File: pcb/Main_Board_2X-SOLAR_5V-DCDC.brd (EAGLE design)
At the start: 86.4 x 52.1 mm, 89 parts, among them CN1 DCIN, CN5 USBA_FEMALE, CN6 MicroUSB, IC1 MCP73871, IC2 MCP73871, T2 MMUN2133LT1G, U3 TPS61090RSAR

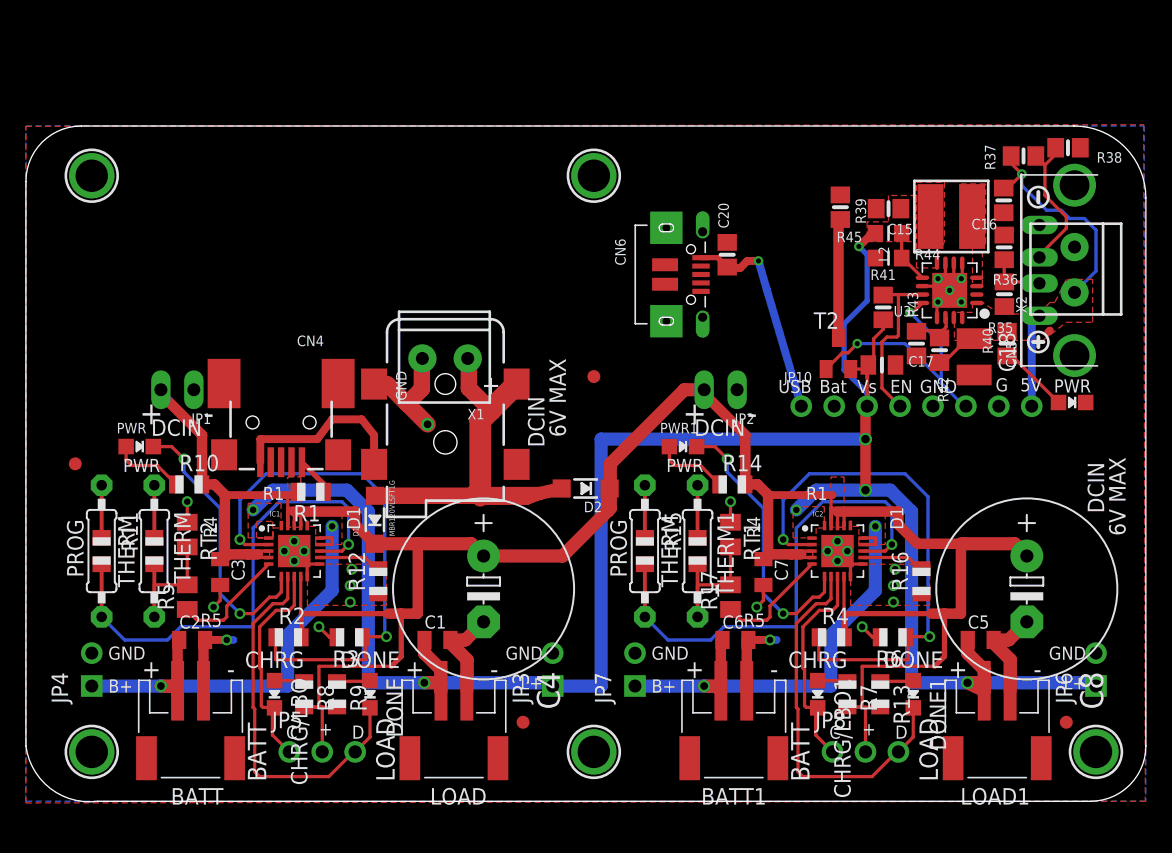
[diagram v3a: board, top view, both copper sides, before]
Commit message: Rev 2 start
Removed extra USB mounts, jumpers, and headers. BOM completed but missing a couple items from Digikey
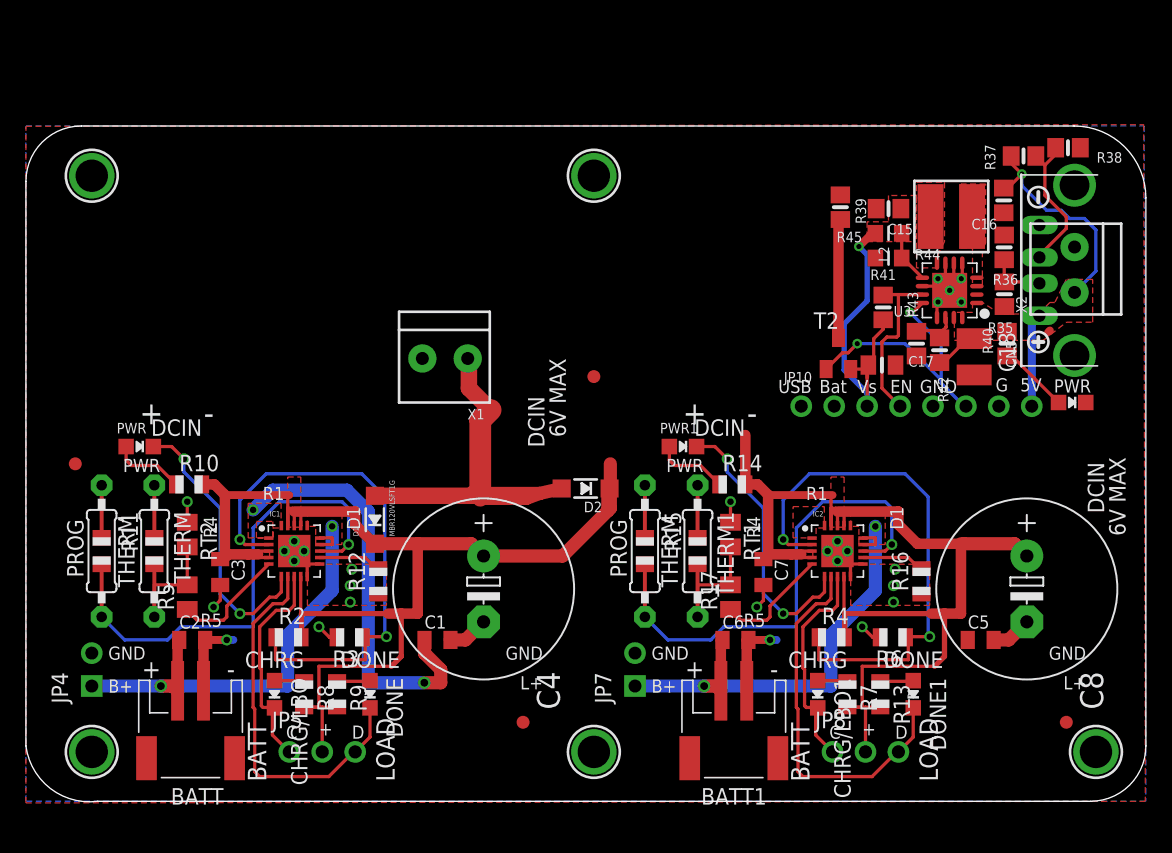
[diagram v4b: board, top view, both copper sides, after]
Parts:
- removed C20: 10uF, microbuilder:0805-NO
- removed CN1: DCIN, microbuilder:DCJACK_2MM_SMT
- removed CN4: (no value), microbuilder:USB-MINIB_LARGER
- removed CN6: MicroUSB, microbuilder:4UCONN_20329
- removed JP1, JP2: DCIN, microbuilder:1X02_OVAL
- removed JP3, JP6: LOAD, microbuilder:1X02_ROUND
- removed LOAD, LOAD1: (no value), adafruit:JST-PH-2-SMT-RA
- removed R1: 0, adafruit:R0805
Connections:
- removed net GNDBREAK: CN1.GNDBREAK, CN4.GND, CN4.GND1, CN4.GND2, CN4.GND3, CN4.GND4
- removed net N$2: CN4.VBUS, R1.1
- net GND: no longer C20.2, CN1.GND, CN6.BASE@1, CN6.BASE@2, CN6.GND, CN6.SPRT@1, CN6.SPRT@2, CN6.SPRT@3, CN6.SPRT@4, JP1.1, JP2.1, JP3.2, JP6.2, LOAD.2, LOAD1.2
- net PV_IN: no longer CN1.PWR
- net VBAT: no longer JP3.1, JP6.1, LOAD.1, LOAD1.1
- net VBUS: no longer C20.1, CN6.VBUS
- net VCC: no longer JP1.2, JP2.2, R1.2
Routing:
- net VBAT: track 162.8 -> 57.3 mm, vias 7 -> 3
- net GND: track 68.9 -> 44.9 mm, vias 23 -> 22
- net VCC: track 209.3 -> 186.2 mm
- net VBUS: track 16.7 -> 0.00 mm, vias 1 -> 0
- net GNDBREAK: track 14.3 -> 0.00 mm
- net N$2: track 2.98 -> 0.00 mm
- net PV_IN: track 34.4 -> 31.5 mm

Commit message: Part removal and gitignore update
removed more jumpers and headers and updated the ignore file to ignore autosave files
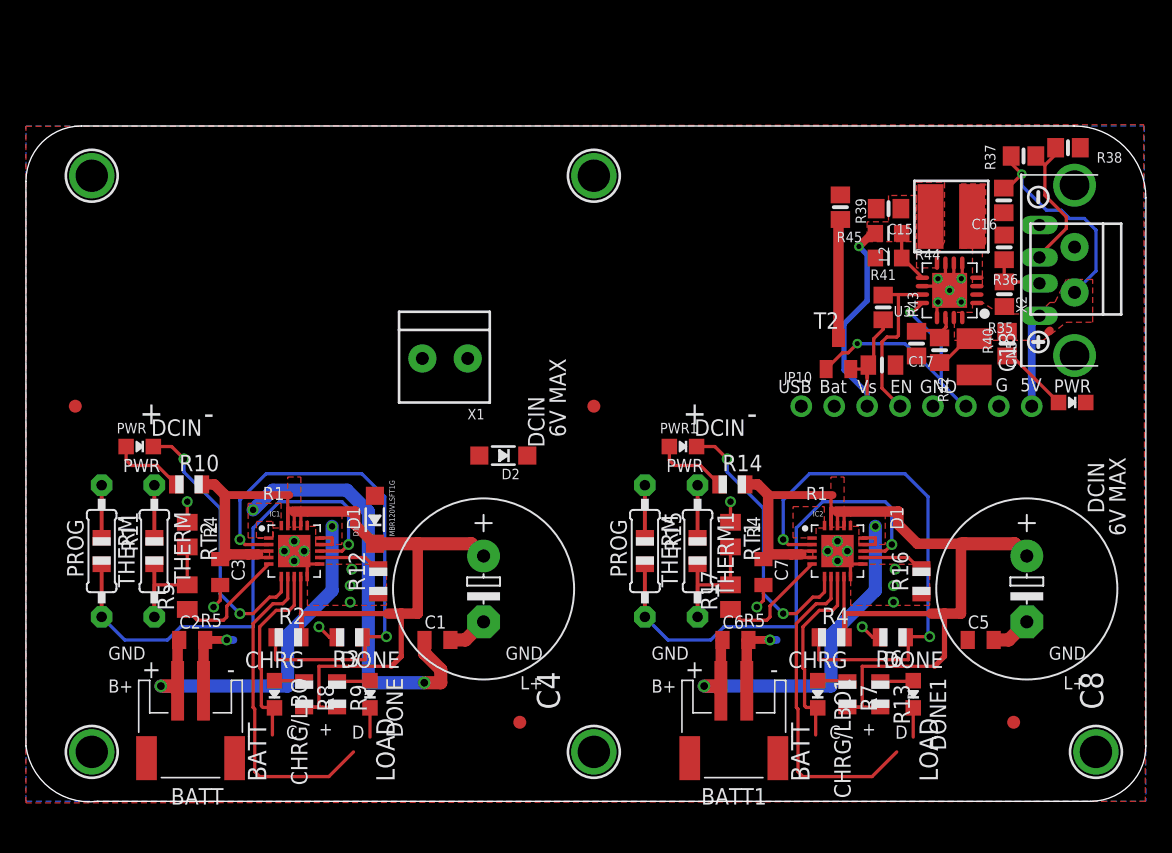
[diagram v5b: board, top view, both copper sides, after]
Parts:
- removed JP4, JP7: BATT, microbuilder:1X02_ROUND
- removed JP5, JP8: (no value), adafruit:1X03-CLEANBIG
- moved D2 6.84 mm to (36.8, 26.7)
- moved U$2 4.45 mm to (3.81, 30.5)
- moved U$10 4.06 mm to (76.2, 6.10)
- moved U$8 2.29 mm to (43.8, 30.5)
- moved U$3 0.25 mm to (38.1, 6.10)
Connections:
- net BATT: no longer JP4.1
- net BATT1: no longer JP7.1
- net GND: no longer JP4.2, JP7.2
- net N$11: no longer JP5.1
- net N$17: no longer JP8.3
- net N$18: no longer JP8.1
- net N$4: no longer JP5.3
- net VCC: no longer JP5.2, JP8.2
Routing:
- net PV_IN: track 31.5 -> 0.00 mm
- net VCC: track 186.2 -> 159.0 mm
- net BATT1: track 37.0 -> 31.7 mm
- net BATT: track 37.0 -> 31.7 mm
- net N$11: track 16.8 -> 15.0 mm
- net N$18: track 16.8 -> 15.0 mm
- net N$4: track 29.2 -> 27.5 mm
- net N$17: track 29.2 -> 27.5 mm

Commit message: Added jumpers and diodes to load line regulation
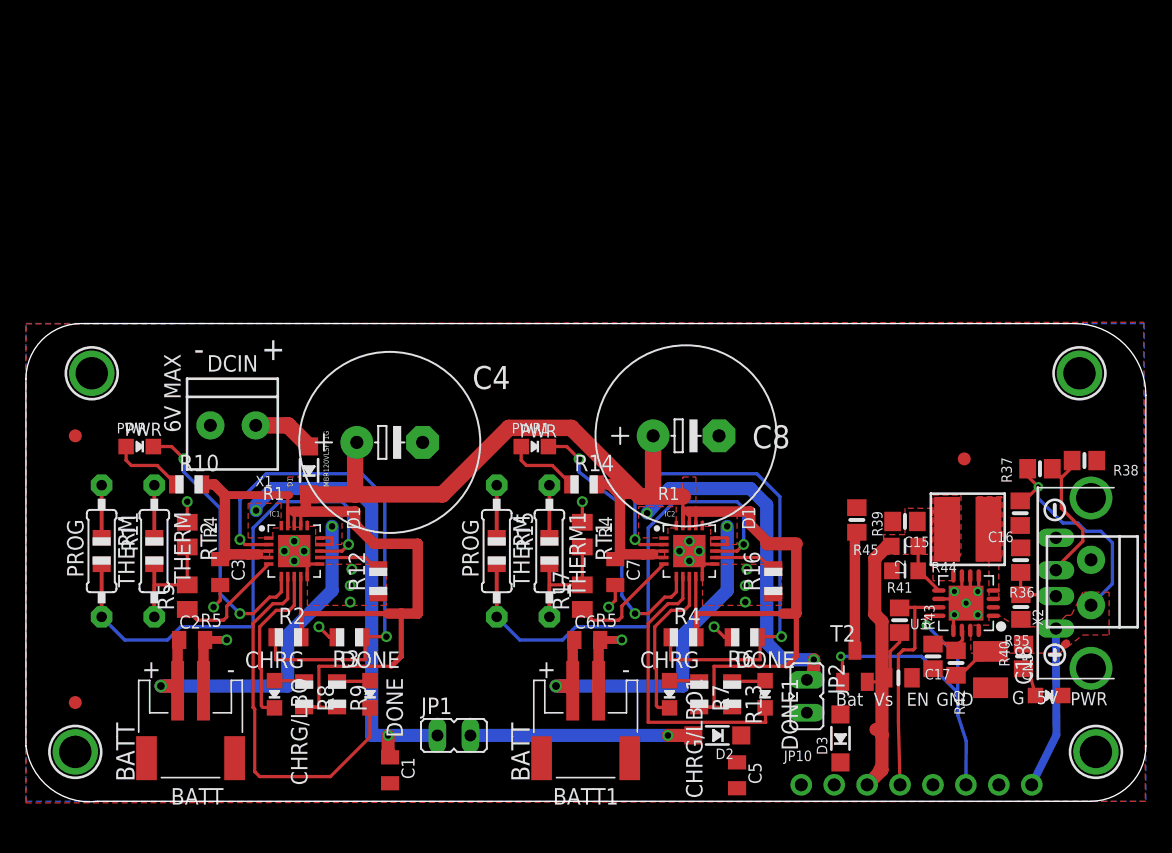
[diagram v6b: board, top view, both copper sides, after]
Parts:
- removed U$2: FIDUCIAL, adafruit:FIDUCIAL_1MM
- removed U$5, U$7: MOUNTINGHOLE2.5, microbuilder:MOUNTINGHOLE_2.5_PLATED
- added D3: MBR120VLSFT1G, microbuilder:SOD-123
- added JP1, JP2: (no value), jumper:JP1
- added U$1: MOUNTINGHOLE2.5, microbuilder:MOUNTINGHOLE_2.5_PLATED
- BATT, BATT1: value (none) -> 3.7V Li-ion
- JP10: value (none) -> 5V step up jumpers
- X1: value (none) -> Solar input
- X2: value (none) -> 5V output
- moved U$10 75.7 mm to (3.81, 28.2)
- moved U$8 46.1 mm to (3.81, 7.62)
- moved U$3 39.9 mm to (72.4, 26.4)
- moved JP10 29.2 mm to (68.7, 1.27)
- moved C8 28.8 mm to (50.9, 28.2), turned to 0 degrees
- moved D2 27.2 mm to (53.3, 5.08)
- moved C17 24.2 mm to (67.3, 9.53)
- moved CN5 24.2 mm to (86.0, 16.8)
- moved R42 24.2 mm to (71.8, 10.7)
- moved U$87 24.2 mm to (79.4, 22.5)
- moved X2 24.2 mm to (82.2, 16.8)
- moved C15 24.2 mm to (67.8, 21.6)
- moved C18 24.2 mm to (74.4, 10.2)
- moved R37 24.2 mm to (78.2, 25.7)
- moved R39 24.2 mm to (64.1, 21.7)
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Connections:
- net LBO renamed T2-BASE_LBO
- net N$1 renamed PG
- net N$11 renamed STAT1
- net N$15 renamed PROG3
- net N$16 renamed PROG1
- net N$17 renamed STAT2_1
- net N$18 renamed STAT1_1
- net N$22 renamed PROG3_1
- net N$23 renamed PROG1_1
- net N$26 renamed T2-DRAIN
- net N$4 renamed STAT2
- net N$9 renamed PG_1
- new net N$1: D3.A, JP2.2
- new net N$2: D2.A, JP1.2
- new net VOUT: C1.1, IC1.P$1, IC1.P$20, JP1.1
- new net VOUT1: C5.1, IC2.P$1, IC2.P$20, JP2.1
- net PV_IN: no longer D2.A
- net VBAT: now also D2.C, D3.C; no longer C1.1, C5.1, IC1.P$1, IC1.P$20, IC2.P$1, IC2.P$20
- net VCC: no longer D2.C
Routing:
- net VOUT: track 0.00 -> 35.0 mm, vias 0 -> 2
- net VCC: track 159.0 -> 188.8 mm
- net VOUT1: track 0.00 -> 27.2 mm, vias 0 -> 2
- net VBAT: track 57.3 -> 34.4 mm, vias 3 -> 0
- net N$2: track 0.00 -> 17.2 mm, vias 0 -> 1
- net GND: track 44.9 -> 37.6 mm
- net T2-BASE_LBO: track 21.2 -> 27.5 mm
- net 5.0V: track 29.2 -> 34.5 mm
- net PV_IN: track 0.00 -> 4.79 mm
- net STAT2_1: track 27.5 -> 23.0 mm
- net ENABLE: track 13.2 -> 17.7 mm
- net N$44: track 5.46 -> 2.52 mm
- net STAT1_1: track 15.0 -> 13.0 mm
- net STAT1: track 15.0 -> 13.0 mm
- net STAT2: track 27.5 -> 29.2 mm
- added copper zone on layer 1, net VOUT
- added copper zone on layer 1, net VOUT1
- removed copper zone on layer 1, net N$3
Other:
- board size 86.4 x 52.1 mm -> 86.4 x 36.9 mm
- board text removed: "B+"
- board text removed: "C"
- board text removed: "D"
- board text removed: "L+"
- board text removed: "LOAD"

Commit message: Cleaned up silkscreen
Moved silkscreen for better visibility during assembly and deleted extra labels. Shrank board a little bit smaller in dimension
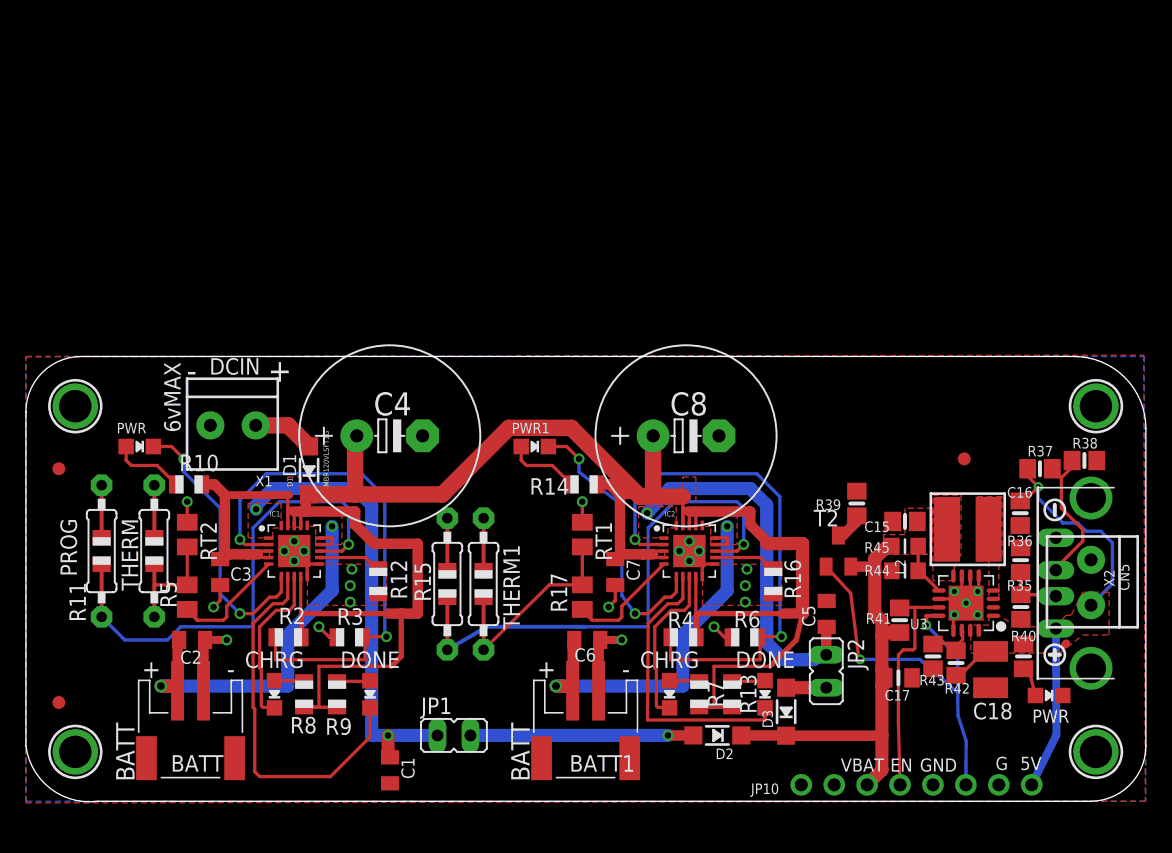
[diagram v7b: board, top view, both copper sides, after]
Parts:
- moved C5 14.2 mm to (61.8, 14.5), turned to 90 degrees
- moved T2 8.98 mm to (62.7, 19.3)
- moved THERM1 5.68 mm to (35.3, 16.8)
- moved D3 4.67 mm to (58.6, 6.91)
- moved R15 4.58 mm to (32.5, 16.8)
- moved U$6 2.84 mm to (3.81, 30.5)
- moved U$1 2.84 mm to (82.5, 30.5)
- moved U$10 2.84 mm to (2.54, 25.7)
- moved JP2 2.44 mm to (61.7, 10.0)
- moved U$8 1.27 mm to (2.54, 7.62)
- moved R39 1.27 mm to (64.1, 23.0)
- moved C4 0.51 mm to (28.1, 28.2)
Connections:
- net N$1 renamed DIODE_PROT_1
- net N$2 renamed DIODE_PROT
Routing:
- net T2-DRAIN: track 9.28 -> 2.28 mm
- net N$25: track 7.94 -> 12.6 mm
- net T2-BASE_LBO: track 27.5 -> 31.9 mm
- net PROG1_1: track 34.1 -> 38.0 mm
- net DIODE_PROT_1: track 0.00 -> 3.10 mm
- net VOUT1: track 27.2 -> 28.7 mm, vias 2 -> 1
- net VBAT: track 34.4 -> 35.7 mm
- net VCC: track 188.8 -> 189.5 mm
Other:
- board size 86.4 x 36.9 mm -> 86.4 x 34.4 mm
- board text added: "+6V"
- board text added: "5Vout: ~5.2V @ 1A+"
- board text added: "6vMAX"
- board text added: "LiPoly 3.7-4.2 V only!"
- board text added: "VBAT"
- board text added: "Vbat"
- board text removed: "5Vout: ~5.2V @ 1A+ output"
- board text removed: "6V MAX"
- board text removed: "BATT+"
- board text removed: "Bat"
- board text removed: "LOAD+"
- board text removed: "LiPo"
- board text removed: "LiPoly: 3.7V/4.2V Li only!"
- board text removed: "R1"
- board text removed: "R4"
- board text removed: "R5"
- board text removed: "THERM"
- board text removed: "USB"
- board text removed: "Vs"
- board text removed: "Vsh"
